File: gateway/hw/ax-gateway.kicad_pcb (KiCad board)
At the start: 2 copper layers, 65 x 56 mm, 90 parts, among them IC1 TG-5006CJ, IC2 TPS73433, IC3 AX5243, IC4 AX5243, P1 Raspberry_Pi_Conn, P2 COAX, P3 COAX, P4 PAD

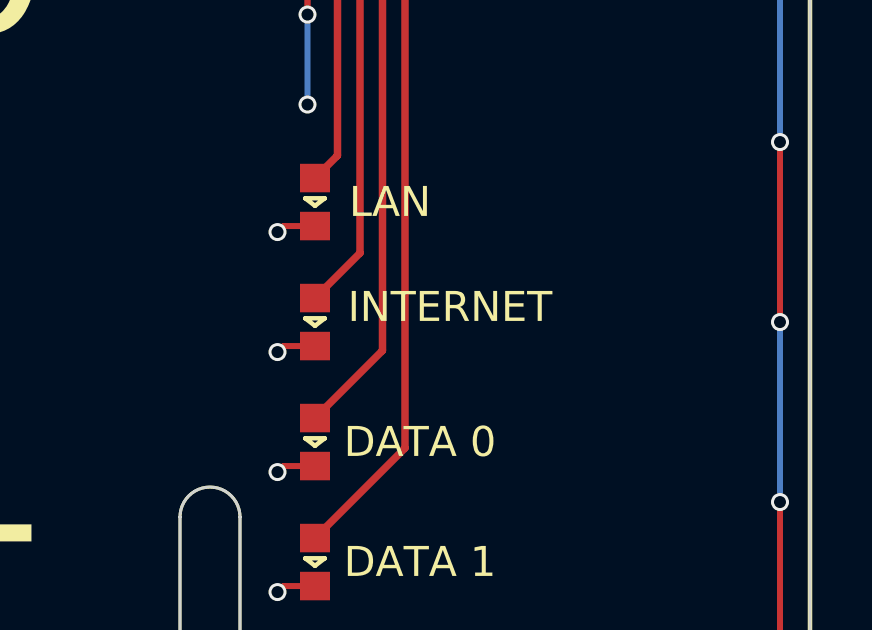
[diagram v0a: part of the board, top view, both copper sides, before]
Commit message: [gateway] fix farnell code for shield
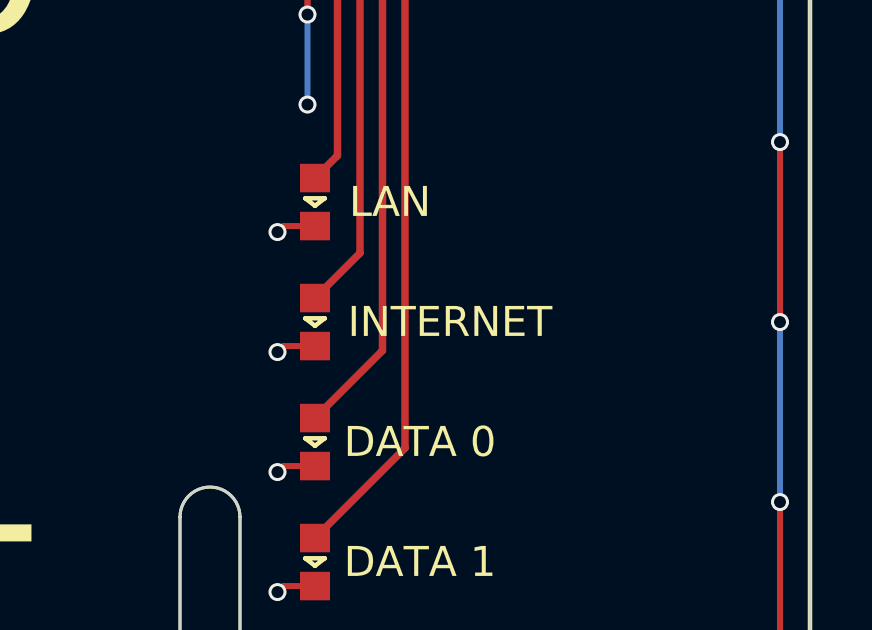
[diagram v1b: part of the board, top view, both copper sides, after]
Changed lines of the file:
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@@
     (links 219)
     (no_connects 1)
-    (area 137.994999 84.375 212.775001 142.775001)
+    (area 147.449999 86.449999 212.550001 142.550001)
     (thickness 1.6)
-    (drawings 26)
+    (drawings 25)
     (tracks 869)
     (zones 0)
@@
       (effects (font (size 1 1) (thickness 0.15)))
     )
-    (fp_text value Raspberry_Pi_Conn (at -23 -4.5) (layer F.Fab)
+    (fp_text value Raspberry_Pi_Conn (at -23 -4.5) (layer F.Fab) hide
       (effects (font (size 1 1) (thickness 0.15)))
     )
@@
       (effects (font (size 1 1) (thickness 0.15)))
     )
-    (fp_text value INTERNET (at 0.5 4.5 180) (layer F.SilkS)
+    (fp_text value INTERNET (at 0 4.5 180) (layer F.SilkS)
       (effects (font (size 1 1) (thickness 0.15)))
     )
@@
       (net 4 GND) (zone_connect 2))
   )
-  (dimension 14 (width 0.3) (layer Eco1.User)
-    (gr_text "14.000 mm" (at 207.35 119 270) (layer Eco1.User)
-      (effects (font (size 1.5 1.5) (thickness 0.3)))
-    )
-    (feature1 (pts (xy 200 126) (xy 208.7 126)))
-    (feature2 (pts (xy 200 112) (xy 208.7 112)))
-    (crossbar (pts (xy 206 112) (xy 206 126)))
-    (arrow1a (pts (xy 206 126) (xy 205.413579 124.873496)))
-    (arrow1b (pts (xy 206 126) (xy 206.586421 124.873496)))
-    (arrow2a (pts (xy 206 112) (xy 205.413579 113.126504)))
-    (arrow2b (pts (xy 206 112) (xy 206.586421 113.126504)))
-  )
   (gr_text "DC 1" (at 163 116.75) (layer B.SilkS)

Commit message: [hw] add l_ext
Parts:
- added L17: 0Ω, agg:0402, F.Cu at (171.8, 108.0)
- added L18: 0Ω, agg:0402, F.Cu at (172.2, 126.0)
- moved C15 0.25 mm to (170.2, 108.2)
- moved C18 0.25 mm to (170.8, 126.2)
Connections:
- IC3 pad 7: /SYNTH_LOOP_0 -> /L1_0
- IC3 pad 8: /SYNTH_LOOP_0 -> /L2_0
- IC4 pad 7: /SYNTH_LOOP_1 -> /L1_1
- IC4 pad 8: /SYNTH_LOOP_1 -> /L2_1
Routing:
- net /L2_1: track 0.00 -> 1.94 mm
- net /L2_0: track 0.00 -> 1.94 mm
- net /L1_1: track 0.00 -> 1.77 mm
- net /L1_0: track 0.00 -> 1.77 mm
- net /SYNTH_LOOP_1: track 0.50 -> 0.00 mm
- net /SYNTH_LOOP_0: track 0.50 -> 0.00 mm

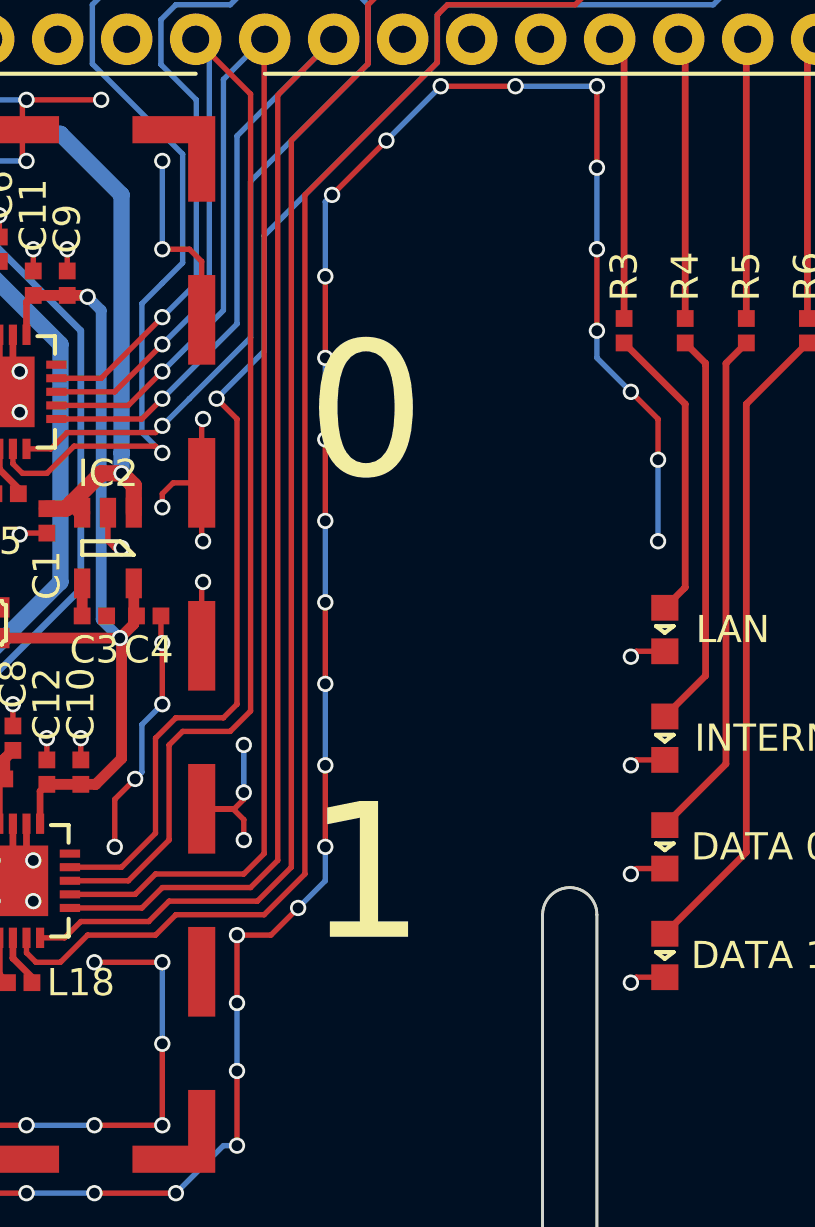
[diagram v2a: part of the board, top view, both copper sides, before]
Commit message: [hw] add silk fields for noting frequency
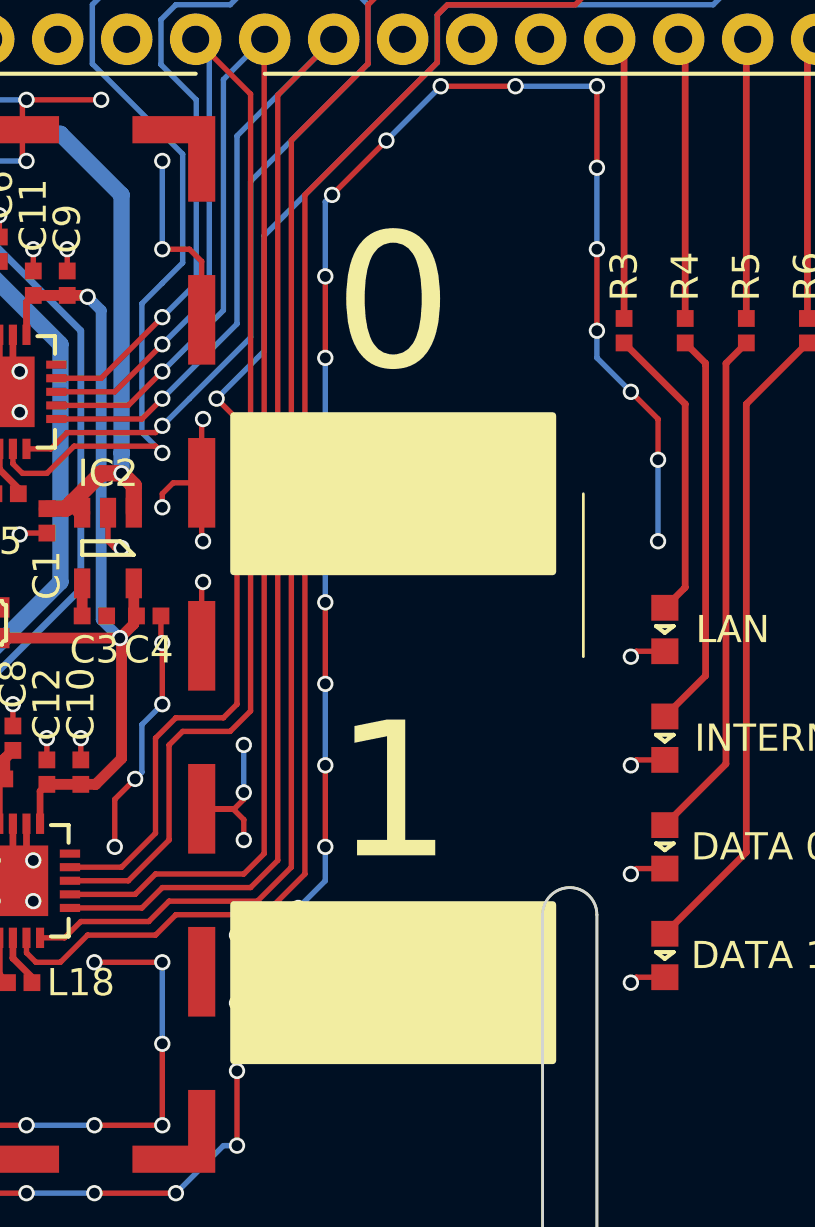
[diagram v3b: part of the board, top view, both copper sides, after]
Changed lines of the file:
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@@
     (area 147.449999 86.449999 212.550001 142.550001)
     (thickness 1.6)
-    (drawings 25)
+    (drawings 26)
     (tracks 879)
     (zones 0)
@@
     )
   )
+  (gr_line (start 193 108) (end 193 114) (angle 90) (layer F.SilkS) (width 0.1))
   (gr_text "DC 1" (at 163 116.75) (layer B.SilkS)
     (effects (font (size 1 1) (thickness 0.15)) (justify mirror))
@@
     (effects (font (size 1 1) (thickness 0.15)))
   )
-  (gr_text 1 (at 185 122) (layer F.SilkS)
+  (gr_text 1 (at 186 119) (layer F.SilkS)
     (effects (font (size 5 5) (thickness 0.8)))
   )
-  (gr_text 0 (at 185 105) (layer F.SilkS)
+  (gr_text 0 (at 186 101) (layer F.SilkS)
     (effects (font (size 5 5) (thickness 0.8)))
   )
@@
       )
     )
+  )
+  (zone (net 0) (net_name "") (layer F.SilkS) (hatch edge 0.508)
+    (connect_pads (clearance 0.5))
+    (min_thickness 0.254)
+    (fill yes (arc_segments 16) (thermal_gap 0.508) (thermal_bridge_width 0.508))
+    (polygon
+      (pts
+        (xy 192 111) (xy 180 111) (xy 180 105) (xy 192 105) (xy 192 111)
+      )
+    )
+  )
+  (zone (net 0) (net_name "") (layer F.SilkS) (hatch edge 0.508)
+    (connect_pads (clearance 0.5))
+    (min_thickness 0.254)
+    (fill yes (arc_segments 16) (thermal_gap 0.508) (thermal_bridge_width 0.508))
+    (polygon
+      (pts
+        (xy 192 129) (xy 180 129) (xy 180 123) (xy 192 123) (xy 192 129)
+      )
+    )

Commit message: [pi hw] add l_ext
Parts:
- L17, L18: value 0Ω -> 22nH; footprint agg:0402 -> agg:0603
- moved C1 4.04 mm to (177.0, 107.5), turned to 0 degrees
- moved L17 0.71 mm to (172.2, 108.5)
- moved L18 0.71 mm to (172.8, 126.5)
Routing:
- net GND: track 475.9 -> 477.0 mm, vias 191 -> 192
- net VDD: track 79.8 -> 78.8 mm
- net /L2_1: track 1.94 -> 2.82 mm
- net /L2_0: track 1.94 -> 2.82 mm
- net /L1_1: track 1.77 -> 2.34 mm
- net /L1_0: track 1.77 -> 2.34 mm
- net (no net): vias 2 -> 0
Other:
- board text added: "Richard Meadows"
- board text added: "ax gateway v0.4 15-11-16"
